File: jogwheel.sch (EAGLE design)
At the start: 61 parts, among them IC1 FT232RL

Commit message: Parts in are in correct places (4 line opto version).
Few traces done. Not many however.
Fixed silkscreen slightly.
First version ordered from iteadstudios.
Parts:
- removed 2.U0, 2.U1, 5.U0: OPTO_2_CHANNELSACPL-827-300E, jogwheel_parts:OPTO_2_CHANNELSACPL-827-300E
- removed 8.T0, 8.T1, 8.T2, 8.T3, 8.T4, 8.T5, 8.T6, 8.T7: CONNECTOR_2PIN2W-TERMINAL-HEADER-20.155MV/2, connectors:CONNECTOR_2PIN2W-TERMINAL-HEADER-20.155MV/2
- removed C5: 100nF, RC_and_L:C-EUC0805
- added 1.C4: 100nF, RC_and_L:C-EUC0805
- added 5.R10, 5.R11, 5.R12, 5.R13, 5.R14, 5.R15, 5.R16, 5.R17, 5.R18, 5.R19, 5.R20, 5.R21, 5.R22, 5.R23, 5.R4, 5.R5, 5.R6, 5.R7, 5.R8, 5.R9: 10k, RC_and_L:R-EU_R0805
- added 5.T10, 5.T11, 5.T2, 5.T3, 5.T4, 5.T5, 5.T6, 5.T7, 5.T8, 5.T9: CONNECTOR_2PIN2W-TERMINAL-HEADER-20.155MV/2, connectors:CONNECTOR_2PIN2W-TERMINAL-HEADER-20.155MV/2
- added IC2, IC3, IC4, IC5: OPTO_4_CHANNELS, jogwheel_parts:OPTO_4_CHANNELS
- 4.T4: PIN1 24V_IN -> AGND; PIN2 AGND -> 24VIN
- 6.T0: PIN2 (none) -> GND
- 6.T2: PIN2 (none) -> AREF
- 6.T4, 6.T5, 6.T6: PIN2 (none) -> AGND
- 6.T7, 6.T8: PIN1 (none) -> 24V
- renumbered C1 to 0.C4, C3 to 0.C3
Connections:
- net N$13 renamed AVCC
- removed net VCC: 0.C0.+, 0.C1.1
- new net N$12: 5.R4.1, IC3_G3.AN
- new net N$14: 5.R5.1, IC3_G4.AN
- new net N$25: 5.T3.P$2, IC3_G4.CA
- new net N$26: 5.R5.2, 5.T3.P$1
- new net N$27: 5.T2.P$2, IC3_G3.CA
- new net N$28: 5.R4.2, 5.T2.P$1
- new net N$29: 5.R8.1, IC4_G1.AN
- new net N$30: 5.R10.1, IC4_G2.AN
- new net N$31: 5.T5.P$2, IC4_G2.CA
- new net N$32: 5.R10.2, 5.T5.P$1
- new net N$33: 5.T4.P$2, IC4_G1.CA
- new net N$34: 5.R8.2, 5.T4.P$1
- new net N$35: 5.R12.1, IC4_G3.AN
- new net N$36: 5.R13.1, IC4_G4.AN
- new net N$37: 5.T7.P$2, IC4_G4.CA
- new net N$38: 5.R13.2, 5.T7.P$1
- new net N$39: 5.T6.P$2, IC4_G3.CA
- new net N$40: 5.R12.2, 5.T6.P$1
- new net N$41: 5.R16.1, IC5_G1.AN
- new net N$42: 5.R18.1, IC5_G2.AN
- new net N$43: 5.T9.P$2, IC5_G2.CA
- new net N$44: 5.R18.2, 5.T9.P$1
- new net N$45: 5.T8.P$2, IC5_G1.CA
- new net N$46: 5.R16.2, 5.T8.P$1
- new net N$47: 5.R20.1, IC5_G3.AN
- new net N$48: 5.R21.1, IC5_G4.AN
- new net N$49: 5.T11.P$2, IC5_G4.CA
- new net N$50: 5.R21.2, 5.T11.P$1
- new net N$51: 5.T10.P$2, IC5_G3.CA
- new net N$52: 5.R20.2, 5.T10.P$1
- net +24V: now also 4.T4.P$2, IC2_G1.C, IC2_G2.C, IC2_G3.C, IC2_G4.C; no longer 2.U0_G1.C, 2.U0_G2.C, 2.U1_G1.C, 2.U1_G2.C, 4.T4.P$1
- net +3V3: now also 1.C4.1; no longer 0.C2.1
- net +5V: now also 0.C0.+, 0.C1.1, 0.C2.1, IC3_G1.C, IC3_G2.C, IC3_G3.C, IC3_G4.C, IC4_G1.C, IC4_G2.C, IC4_G3.C, IC4_G4.C, IC5_G1.C, IC5_G2.C, IC5_G3.C, IC5_G4.C; no longer 5.U0_G1.C, 5.U0_G2.C, C5.1
- net AGND: now also 4.T4.P$1; no longer 4.T4.P$2
- net B2: now also 5.R14.1, IC4_G3.E
- net C0: now also 5.R15.1, IC4_G4.E; no longer 8.T0.P$2
- net C1: now also 5.R17.1, IC5_G1.E; no longer 8.T1.P$2
- net C2: now also 5.R19.1, IC5_G2.E; no longer 8.T2.P$2
- net C3: now also 5.R22.1, IC5_G3.E; no longer 8.T3.P$2
- net C4: now also 5.R23.1, IC5_G4.E; no longer 8.T4.P$2
- net C5: no longer 8.T5.P$2
- net D2: now also IC3_G1.E; no longer 5.U0_G2.E
- net D3: now also IC3_G2.E; no longer 5.U0_G1.E
- net D4: now also 5.R6.1, IC3_G3.E
- net D5: now also 5.R7.1, IC3_G4.E
- net D6: now also 5.R9.1, IC4_G1.E; no longer 8.T6.P$2
- net D7: now also 5.R11.1, IC4_G2.E; no longer 8.T7.P$2
- net GND: now also 1.C4.2, 5.R11.2, 5.R14.2, 5.R15.2, 5.R17.2, 5.R19.2, 5.R22.2, 5.R23.2, 5.R6.2, 5.R7.2, 5.R9.2, IC2_G1.CA, IC2_G2.CA, IC2_G3.CA, IC2_G4.CA; no longer 2.U0_G1.CA, 2.U0_G2.CA, 2.U1_G1.CA, 2.U1_G2.CA, 8.T0.P$1, 8.T1.P$1, 8.T2.P$1, 8.T3.P$1, 8.T4.P$1, 8.T5.P$1, 8.T6.P$1, 8.T7.P$1, C5.2
- net N$11: now also IC2_G1.E; no longer 2.U0_G2.E
- net N$15: now also IC3_G2.AN; no longer 5.U0_G1.AN
- net N$16: now also IC2_G1.AN; no longer 2.U0_G2.AN
- net N$17: now also IC2_G4.AN; no longer 2.U1_G1.AN
- net N$19: now also IC2_G3.AN; no longer 2.U1_G2.AN
- net N$20: now also IC3_G1.AN; no longer 5.U0_G2.AN
- net N$21: now also IC2_G2.AN; no longer 2.U0_G1.AN
- net N$22: now also IC3_G1.CA; no longer 5.U0_G2.CA
- net N$23: now also IC3_G2.CA; no longer 5.U0_G1.CA
- net N$5: now also IC2_G3.E; no longer 2.U1_G2.E
- net N$6: now also IC2_G4.E; no longer 2.U1_G1.E
- net N$9: now also IC2_G2.E; no longer 2.U0_G1.E
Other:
- note removed: "GPIO [8]"
- moved on the sheet: 0.C2, 4.T4

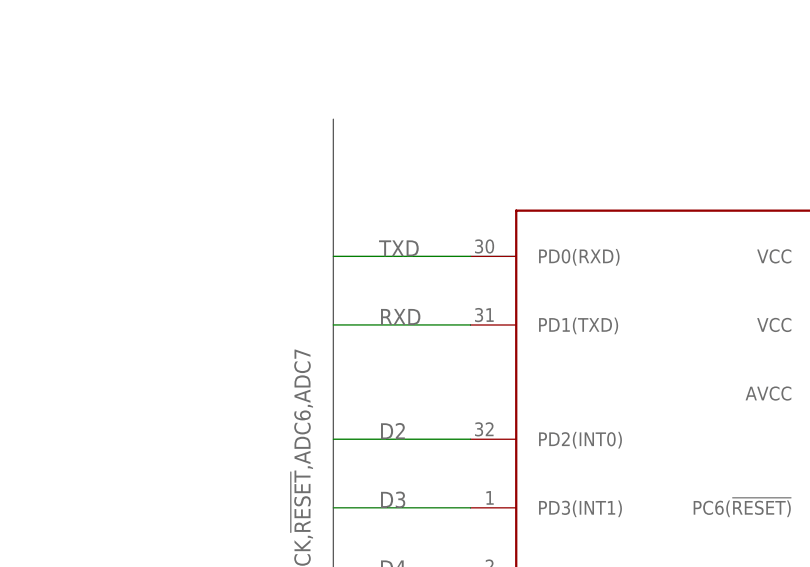
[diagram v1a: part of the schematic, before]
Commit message: Fixed usart txd/rxd error from board.
Accidently, RXD/TXD wasn't crossed...
Now fixed!
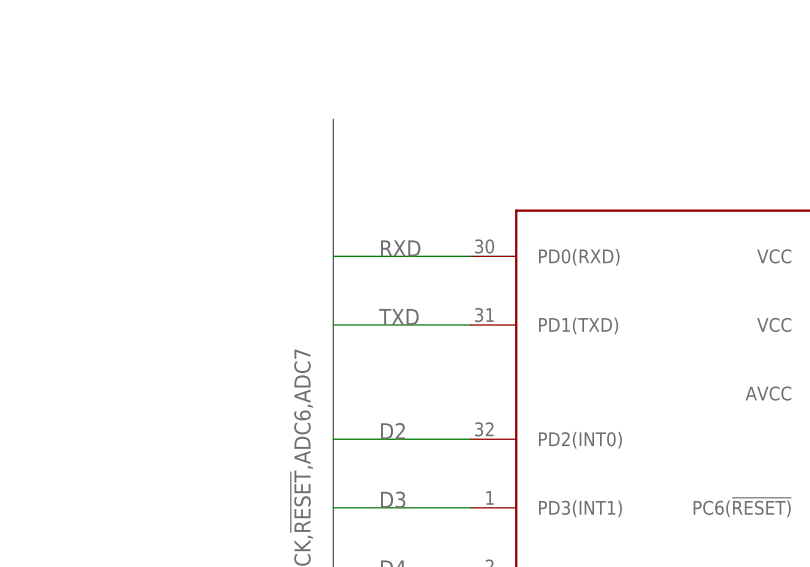
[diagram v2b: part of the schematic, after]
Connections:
- net RXD: now also 1.MCU1.PD0(RXD); no longer 1.MCU1.PD1(TXD)
- net TXD: now also 1.MCU1.PD1(TXD); no longer 1.MCU1.PD0(RXD)
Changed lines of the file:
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@@
 <net name="TXD" class="0">
-<segment>
-<pinref part="1.MCU1" gate="G$1" pin="PD0(RXD)"/>
-<wire x1="111.76" y1="66.04" x2="96.52" y2="66.04" width="0.1524" layer="91"/>
-<label x="101.6" y="66.04" size="1.778" layer="95"/>
-</segment>
 <segment>
 <pinref part="IC1" gate="G$1" pin="RXD"/>
@@
 <label x="-7.62" y="91.44" size="1.778" layer="95"/>
 </segment>
-</net>
-<net name="RXD" class="0">
 <segment>
 <pinref part="1.MCU1" gate="G$1" pin="PD1(TXD)"/>
@@
 <label x="101.6" y="58.42" size="1.778" layer="95"/>
 </segment>
+</net>
+<net name="RXD" class="0">
 <segment>
 <pinref part="IC1" gate="G$1" pin="TXD"/>
@@
 <label x="-7.62" y="86.36" size="1.778" layer="95"/>
 </segment>
+<segment>
+<pinref part="1.MCU1" gate="G$1" pin="PD0(RXD)"/>
+<wire x1="111.76" y1="66.04" x2="96.52" y2="66.04" width="0.1524" layer="91"/>
+<label x="101.6" y="66.04" size="1.778" layer="95"/>
+</segment>
 </net>
